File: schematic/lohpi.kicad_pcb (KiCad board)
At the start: 4 copper layers, 65 x 56 mm, 187 parts, among them J1 CONN_01X02, J10 CONN_01X01, J11 CONN_01X01, J12 CONN_01X01, J13 CONN_01X01, J2 CONN_01X01, J3 CONN_01X01, J4 CONN_01X01, J5 CONN_01X01, J6 CONN_01X01, J8 raspberry_pi_3_header, J9 CONN_01X02, Q1 Q_PMOS_GSD, U1 MCP1726-3302E/SN, U10 Anaren_B0430J50100AHF, U11 MurataSF2314E, U12 MurataSF2314E, U13 SPF5043Z, U14 RFPA0133TR7, U15 MurataSF2314E, U16 RFSW1012, U17 MurataSF2314E, U2 MCP1612, U3 MCP1726-3302E/SN, U4 MCP1824, U5 MCP1824, U6 MCP1824, U7 SX1301, U8 SX1257, U9 SX1257, X1 ABRACON-OSC, X2 ABRACON-OSC

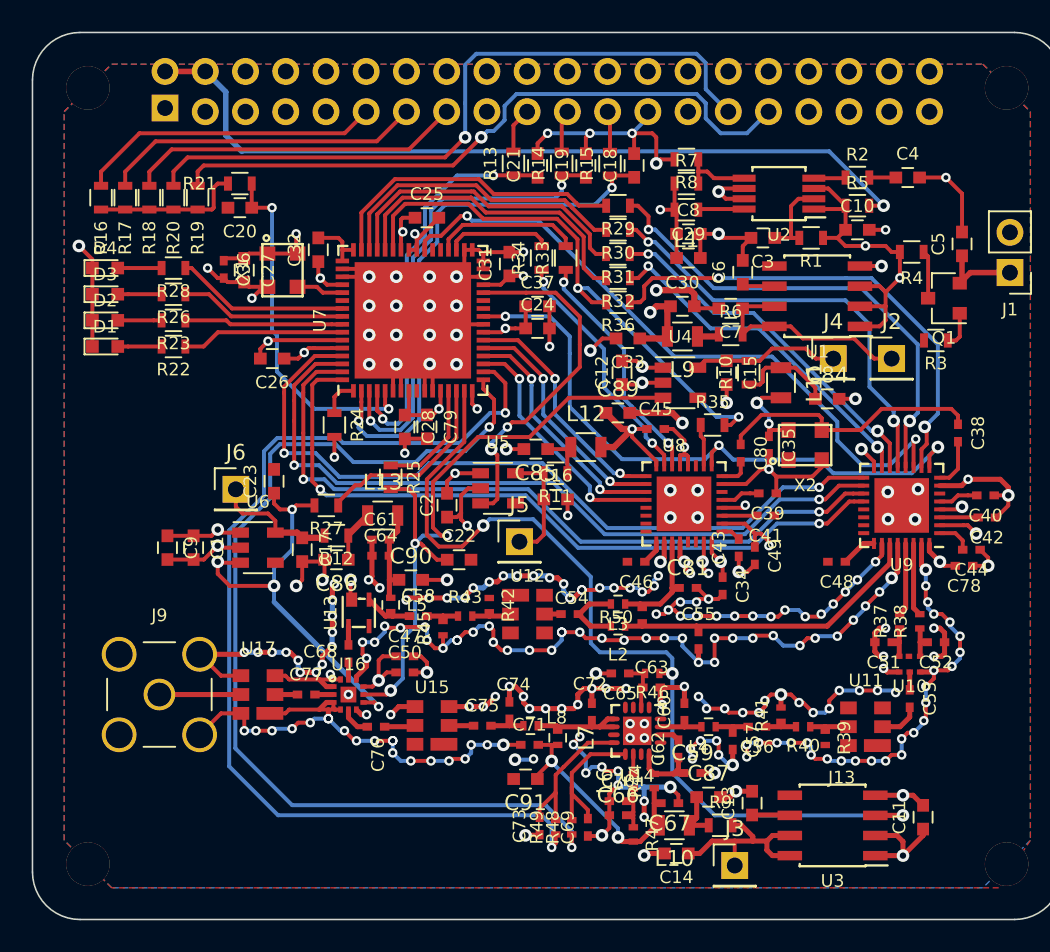
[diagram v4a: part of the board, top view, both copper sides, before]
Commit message: HF layout changed, GPS module added
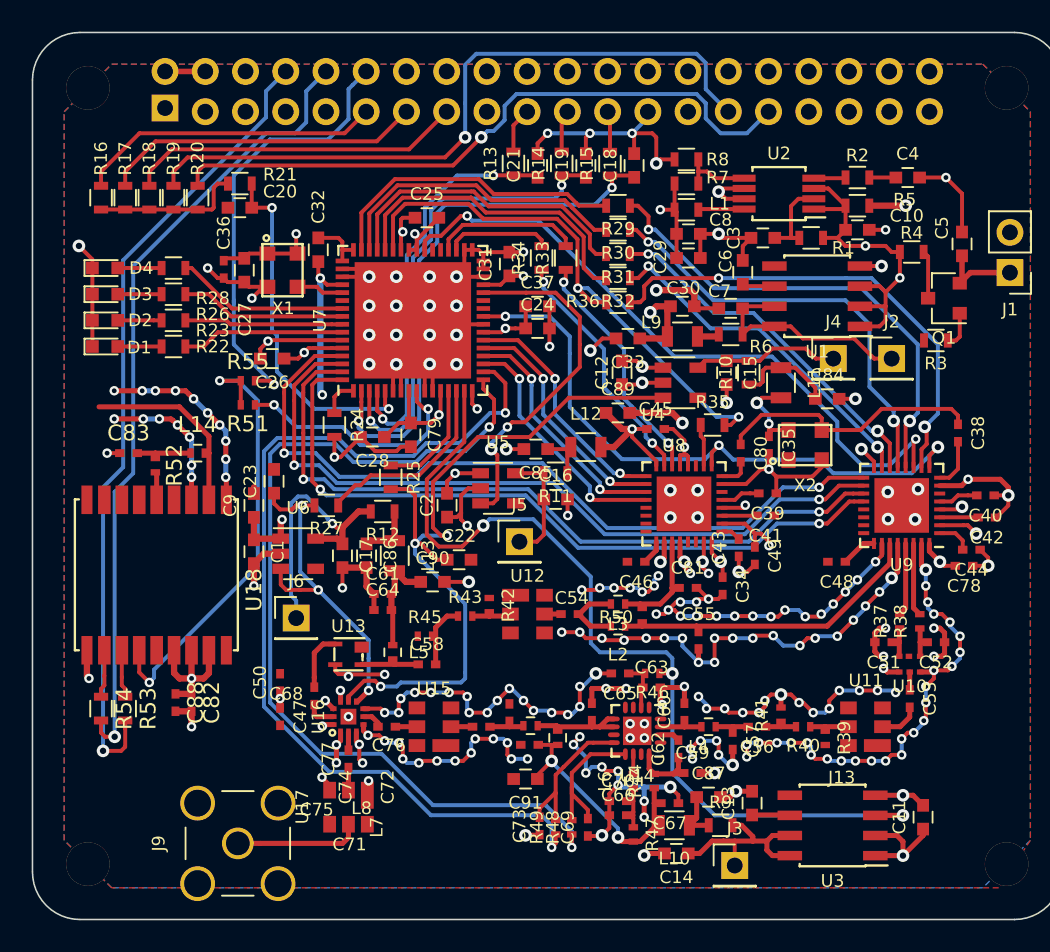
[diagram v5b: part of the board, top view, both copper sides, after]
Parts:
- added C82: 100nF, Capacitors_SMD:C_0402_NoSilk, F.Cu at (98.0, 154.3)
- added C83: 10nF, Capacitors_SMD:C_0402_NoSilk, F.Cu at (94.1, 138.6)
- added C88: 100nF, Capacitors_SMD:C_0402_NoSilk, F.Cu at (97.0, 154.3)
- added L14: 27nH, Inductors_SMD:L_0402, F.Cu at (98.4, 138.6)
- added R51: 100, Resistors_SMD:R_0402_NoSilk, F.Cu at (101.6, 135.5)
- added R52: 10, Resistors_SMD:R_0402_NoSilk, F.Cu at (95.8, 139.3)
- added R53: 100, Resistors_SMD:R_0603, F.Cu at (93.9, 154.7)
- added R54: 100, Resistors_SMD:R_0603, F.Cu at (92.3, 154.7)
- added R55: 100, Resistors_SMD:R_0402_NoSilk, F.Cu at (101.6, 134.0)
- added U18: MAX-M8, max_8:MAX-M8, F.Cu at (91.4, 151.0)
- moved J9 10.6 mm to (101.0, 163.2), turned to 90 degrees
- moved U17 9.12 mm to (108.0, 160.9), turned to 270 degrees
- moved J6 8.98 mm to (104.6, 149.0)
- moved C47 8.75 mm to (103.6, 155.2), turned to 270 degrees
- moved C50 7.90 mm to (103.6, 153.0), turned to 90 degrees
- moved C9 6.08 mm to (102.0, 141.9), turned to 90 degrees
- moved C77 4.86 mm to (108.0, 157.9), turned to 90 degrees
- moved C1 3.82 mm to (102.0, 144.8)
- moved C68 3.43 mm to (105.8, 153.9)
- moved C61 3.43 mm to (110.1, 147.4)
- moved C64 3.43 mm to (110.1, 148.5)
- moved R12 3.29 mm to (110.1, 142.2)
- moved C58 3.10 mm to (112.9, 151.9)
- moved L5 2.99 mm to (110.7, 151.1)
- moved U13 2.69 mm to (108.0, 151.3), turned to 90 degrees
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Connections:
- J10 pad 1: (no net) -> Net-(J10-Pad1)
- J11 pad 1: (no net) -> Net-(J11-Pad1)
- J12 pad 1: (no net) -> Net-(J12-Pad1)
- J13 pad 1: (no net) -> Net-(J13-Pad1)
- J8 pad 1: Net-(J8-Pad1) -> (no net)
- J8 pad 16: Net-(J8-Pad16) -> (no net)
- J8 pad 17: Net-(J8-Pad17) -> (no net)
- J8 pad 18: Net-(J8-Pad18) -> (no net)
- J8 pad 22: Net-(J8-Pad22) -> (no net)
- J8 pad 24: Net-(J8-Pad24) -> (no net)
- J8 pad 26: Net-(J8-Pad26) -> (no net)
- J8 pad 27: Net-(J8-Pad27) -> (no net)
- J8 pad 28: Net-(J8-Pad28) -> (no net)
- J8 pad 3: Net-(J8-Pad3) -> (no net)
- J8 pad 32: Net-(J8-Pad32) -> (no net)
- J8 pad 33: Net-(J8-Pad33) -> (no net)
- J8 pad 35: Net-(J8-Pad35) -> (no net)
- J8 pad 36: Net-(J8-Pad36) -> (no net)
- J8 pad 37: Net-(J8-Pad37) -> (no net)
- J8 pad 38: Net-(J8-Pad38) -> (no net)
- J8 pad 40: Net-(J8-Pad40) -> (no net)
- J8 pad 5: Net-(J8-Pad5) -> (no net)
- J8 pad 7: Net-(J8-Pad7) -> (no net)
- U1 pad 5: Net-(U1-Pad5) -> (no net)
- U10 pad 5: (no net) -> Net-(U10-Pad5)
- U14 pad 1: (no net) -> Net-(U14-Pad1)
- U14 pad 11: (no net) -> Net-(U14-Pad11)
- U14 pad 15: (no net) -> Net-(U14-Pad15)
- U14 pad 4: (no net) -> Net-(U14-Pad4)
- U14 pad 5: (no net) -> Net-(U14-Pad5)
- U14 pad 7: (no net) -> Net-(U14-Pad7)
- U14 pad 8: (no net) -> Net-(U14-Pad8)
- U3 pad 5: Net-(U3-Pad5) -> (no net)
- U4 pad 4: Net-(U4-Pad4) -> (no net)
- U5 pad 4: Net-(U5-Pad4) -> (no net)
- U6 pad 4: Net-(U6-Pad4) -> (no net)
- U7 pad 26: Net-(U7-Pad26) -> (no net)
- U7 pad 27: Net-(U7-Pad27) -> (no net)
- U7 pad 37: Net-(U7-Pad37) -> (no net)
- U7 pad 38: Net-(U7-Pad38) -> (no net)
- U7 pad 54: (no net) -> /main_receiver/GPIO[4]
- U8 pad 11: Net-(U8-Pad11) -> (no net)
- U8 pad 21: Net-(U8-Pad21) -> (no net)
- U8 pad 22: Net-(U8-Pad22) -> (no net)
- U8 pad 23: Net-(U8-Pad23) -> (no net)
- U8 pad 24: Net-(U8-Pad24) -> (no net)
- U8 pad 29: Net-(U8-Pad29) -> (no net)
- U8 pad 30: Net-(U8-Pad30) -> (no net)
- U8 pad 6: Net-(U8-Pad6) -> (no net)
- U9 pad 21: Net-(U9-Pad21) -> (no net)
- U9 pad 22: Net-(U9-Pad22) -> (no net)
- U9 pad 23: Net-(U9-Pad23) -> (no net)
- U9 pad 24: Net-(U9-Pad24) -> (no net)
- U9 pad 6: Net-(U9-Pad6) -> (no net)
- X2 pad 1: (no net) -> Net-(X2-Pad1)
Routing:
- net Net-(J8-Pad8): track 0.00 -> 50.8 mm, vias 0 -> 1
- net Net-(J8-Pad10): track 0.00 -> 50.3 mm, vias 0 -> 1
- net +3V3: track 33.8 -> 71.7 mm, vias 3 -> 5
- net GND: track 525.2 -> 490.9 mm, vias 273 -> 249
- net /power_supply/VCC_RADIO_A: track 53.4 -> 82.2 mm, vias 6 -> 7
- net /main_receiver/1PPS: track 0.00 -> 28.7 mm, vias 0 -> 2
- net Net-(J8-Pad12): track 0.00 -> 28.3 mm, vias 0 -> 1
- net Net-(R51-Pad1): track 0.00 -> 15.4 mm, vias 0 -> 2
- net Net-(J7-Pad1): track 0.00 -> 12.0 mm
- net Net-(C17-Pad1): track 8.01 -> 16.7 mm, vias 0 -> 1
- net /main_receiver/RADIO_A_EN: track 41.9 -> 48.4 mm
- net /main_receiver/LNA_A_EN: track 26.5 -> 21.7 mm, vias 4 -> 3
- net /main_receiver/PA_G16: track 63.6 -> 58.8 mm
- net /main_receiver/PA_G8: track 65.1 -> 60.5 mm
- net Net-(C83-Pad2): track 0.00 -> 3.67 mm
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
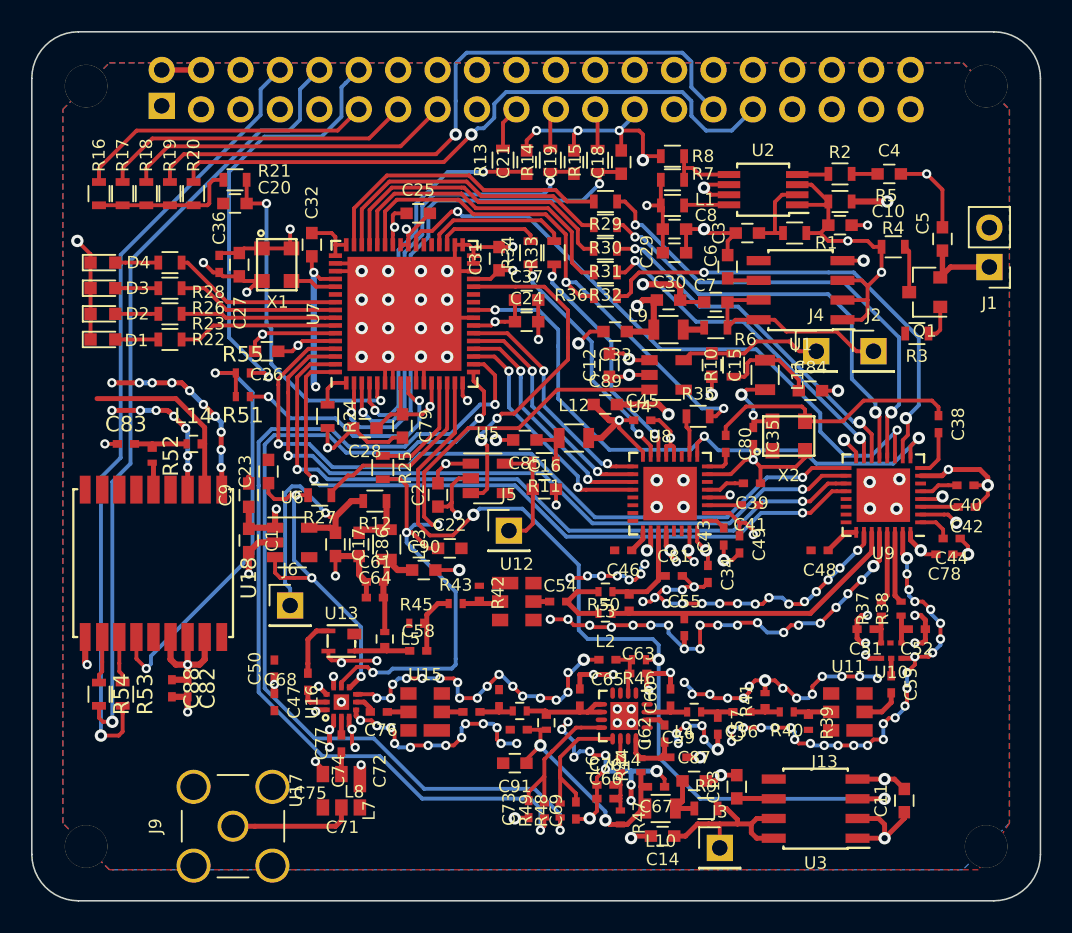
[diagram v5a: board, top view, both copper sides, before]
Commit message: Layout approaching final version. BOM updated
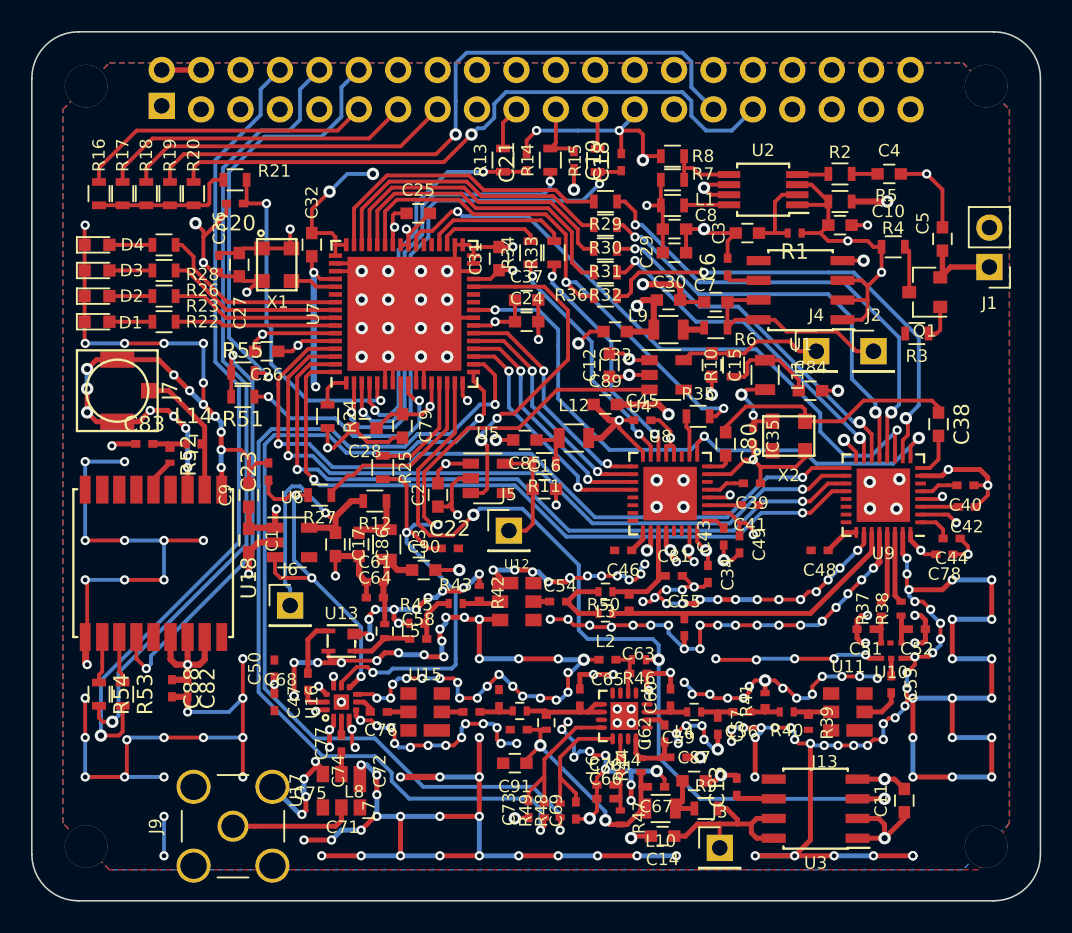
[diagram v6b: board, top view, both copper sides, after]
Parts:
- added J7: UFL, hirose:u.fl, F.Cu at (93.5, 135.1)
- C13, C18, C19, C20, C21, C22, C23, C6: footprint Capacitors_SMD:C_0603 -> Capacitors_SMD:C_0402_NoSilk
- C3, C63: value 0.1uF -> 100nF
- C38: footprint Capacitors_SMD:C_0402_NoSilk -> Capacitors_SMD:C_0603
- C64: value 10000pF -> 100nF
- C78: value 0.01uF -> 10nF
- C80: value 100nF -> 1nF; footprint Capacitors_SMD:C_0402_NoSilk -> Capacitors_SMD:C_0603
- L5: value L -> 100nH
- R1: footprint Resistors_SMD:R_0603 -> Resistors_SMD:R_0402_NoSilk
- R48, R49: value 300 -> 100
- R51, R55: footprint Resistors_SMD:R_0402_NoSilk -> Resistors_SMD:R_0603
- moved D1 1.20 mm to (92.2, 130.7)
- moved D2 1.20 mm to (92.2, 129.0)
- moved D3 1.20 mm to (92.2, 127.4)
- moved D4 1.20 mm to (92.2, 125.7)
- moved R22 1.20 mm to (96.5, 130.7)
- moved R23 1.20 mm to (96.5, 129.0)
- moved R26 1.20 mm to (96.5, 127.4)
- moved R28 1.20 mm to (96.5, 125.7)
- moved C83 1.19 mm to (95.2, 138.6)
- moved R52 1.14 mm to (96.9, 139.3)
- moved C58 0.76 mm to (112.9, 151.1)
- moved L5 0.51 mm to (110.7, 150.6)
- moved C19 0.13 mm to (122.9, 120.3), turned to 270 degrees
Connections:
- C19 pad 1: /main_receiver/MISO -> /main_receiver/RPI_MISO
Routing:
- net GND: track 490.9 -> 770.6 mm, vias 249 -> 360
- net Net-(J7-Pad1): track 12.0 -> 8.67 mm
- net /main_receiver/GPIO[2]: track 10.5 -> 13.3 mm
- net /main_receiver/RPI_MISO: track 2.67 -> 4.78 mm
- net /main_receiver/MISO: track 30.1 -> 28.5 mm
- net /main_receiver/GPIO[3]: track 11.0 -> 12.3 mm
- net Net-(J8-Pad8): track 50.8 -> 52.1 mm
- net Net-(C83-Pad2): track 3.67 -> 2.41 mm
- net Net-(J8-Pad10): track 50.3 -> 51.6 mm
- net /main_receiver/GPIO[1]: track 10.0 -> 10.9 mm
- net Net-(C58-Pad2): track 4.27 -> 3.60 mm
- net Net-(J8-Pad12): track 28.3 -> 27.6 mm
- net /power_supply/VCC_LNA_A: track 6.75 -> 6.24 mm
